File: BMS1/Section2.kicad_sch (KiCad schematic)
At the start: 63 parts

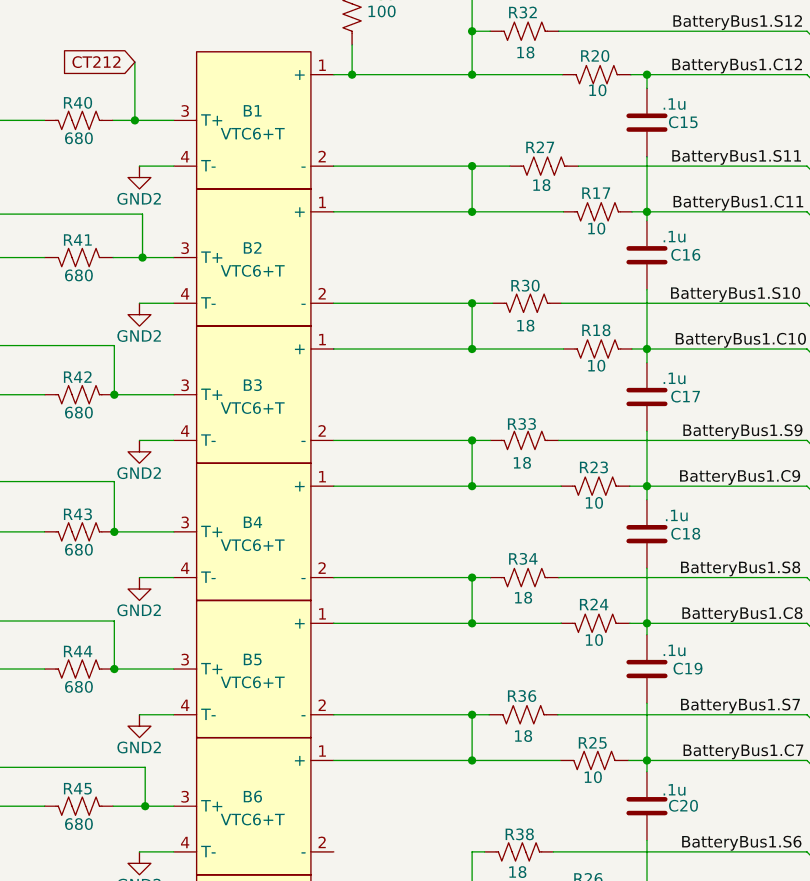
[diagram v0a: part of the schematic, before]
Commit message: added chokes
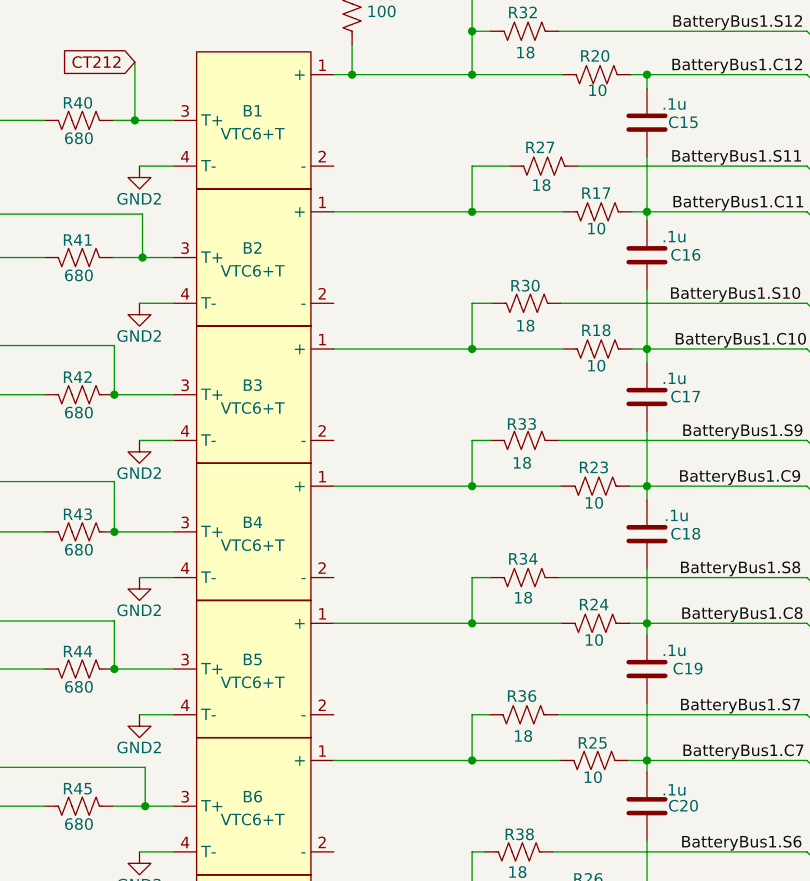
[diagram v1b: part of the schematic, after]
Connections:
- net at B3.1 (+), R18.1, R30.1: no longer B2.2 (-)
- net at B4.1 (+), R23.1, R33.1: no longer B3.2 (-)
- net at B5.1 (+), R24.1, R34.1: no longer B4.2 (-)
- net at B2.1 (+), R17.1, R27.1: no longer B1.2 (-)
- net at B6.1 (+), R25.1, R36.1: no longer B5.2 (-)
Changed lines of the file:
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@@
-	)
-	(junction
-		(at 95.123 67.564)
-		(diameter 0)
-		(color 0 0 0 0)
-	)
-	(junction
-		(at 95.123 82.804)
-		(diameter 0)
-		(color 0 0 0 0)
 	)
 	(junction
@@
 	)
 	(junction
-		(at 95.123 113.284)
-		(diameter 0)
-		(color 0 0 0 0)
-	)
-	(junction
 		(at 114.554 179.324)
 		(diameter 0)
@@
 	)
 	(junction
-		(at 95.123 98.044)
-		(diameter 0)
-		(color 0 0 0 0)
-	)
-	(junction
 		(at 95.123 133.604)
 		(diameter 0)
@@
 	(junction
 		(at 114.554 133.604)
-		(diameter 0)
-		(color 0 0 0 0)
-	)
-	(junction
-		(at 95.123 52.324)
 		(diameter 0)
 		(color 0 0 0 0)
@@
 	(wire
 		(pts
-			(xy 95.123 98.044) (xy 79.756 98.044)
-		)
-		(stroke
-			(width 0)
-			(type default)
-		)
-	)
-	(wire
-		(pts
 			(xy 95.123 148.844) (xy 95.123 143.764)
 		)
@@
 	(wire
 		(pts
-			(xy 79.756 67.564) (xy 95.123 67.564)
-		)
-		(stroke
-			(width 0)
-			(type default)
-		)
-	)
-	(wire
-		(pts
-			(xy 95.123 82.804) (xy 79.756 82.804)
-		)
-		(stroke
-			(width 0)
-			(type default)
-		)
-	)
-	(wire
-		(pts
 			(xy 114.554 72.644) (xy 114.554 74.168)
 		)
@@
 	(wire
 		(pts
-			(xy 95.123 52.324) (xy 79.756 52.324)
-		)
-		(stroke
-			(width 0)
-			(type default)
-		)
-	)
-	(wire
-		(pts
 			(xy 58.4591 169.164) (xy 61.976 169.164)
 		)
@@
 		)
 		(stroke
-			(width 0)
-			(type default)
-		)
-	)
-	(wire
-		(pts
-			(xy 95.123 113.284) (xy 79.756 113.284)
-		)
-		(stroke
